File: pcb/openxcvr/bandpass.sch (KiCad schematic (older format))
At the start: 39 parts, among them U10 SN74CBT3253, U9 SN74CBT3253

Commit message: Candidate design
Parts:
- C30: renamed from C55; value 100nf -> 100n
- C33: renamed from C35; value 100nF -> 100n
- C34: renamed from C36; value 100nF -> 100n
- C35: renamed from C37; value 100nf -> 100n
- C36: renamed from C38; value 100nF -> 100n
- C49: renamed from C51; value 100nF -> 100n
- C50: renamed from C52; value 100nF -> 100n
- C51: renamed from C53; value 100nF -> 100n
- C52: renamed from C54; value 100nF -> 100n
- U8: renamed from U9; value SN74CBT3253 -> FST5253; symbol Analog_Switch:SN74CBT3253 -> xcvr_components:FST5253
- U9: renamed from U10; value SN74CBT3253 -> FST5253; symbol Analog_Switch:SN74CBT3253 -> xcvr_components:FST5253
- renumbered C33 to C31, C34 to C32, C39 to C37, C40 to C38, C41 to C39, C42 to C40, C43 to C41, C44 to C42, C45 to C43, C46 to C44, C47 to C45, C48 to C46, C49 to C47, C50 to C48, R31 to R30, R32 to R31
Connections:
- net labels added: RF_IN
- net labels removed: RF_OUT

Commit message: Get things working with rev 1 PCB
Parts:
- removed U8, U9: FST5253, Package_SO:SOIC-16_3.9x9.9mm_P1.27mm, symbol xcvr_components:FST5253
- added U8, U9: 74LS251, Package_SO:SOIC-16_3.9x9.9mm_P1.27mm, symbol 74xx:74LS251
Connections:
- net +5V: now also U8.16 (VCC), U9.16 (VCC)
- net BAND_0: now also U8.11 (S0), U9.11 (S0)
- net BAND_1: now also U8.10 (S1), U9.10 (S1)
- net BAND_2: now also U8.9 (S2), U9.9 (S2)
- net BPF_16_30_A: now also U8.4 (I0)
- net BPF_16_30_B: now also U9.4 (I0)
- net BPF_2_4_A: now also U8.1 (I3)
- net BPF_2_4_B: now also U9.1 (I3)
- net BPF_4_8_A: now also U8.2 (I2)
- net BPF_4_8_B: now also U9.2 (I2)
- net BPF_8_16_A: now also U8.3 (I1)
- net BPF_8_16_B: now also U9.3 (I1)
- net GND: now also U8.7 (~OE), U8.8 (GND), U9.7 (~OE), U9.8 (GND)
- net RF_BPF: now also U9.5 (Y)
- net at C30.2, R31.2: now also U8.5 (Y)
- new net: U8.12 (I7), U8.13 (I6), U8.14 (I5), U8.15 (I4), U9.12 (I7), U9.13 (I6), U9.14 (I5), U9.15 (I4)
- no-connect marks 4 -> 2
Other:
- moved on the sheet: C30, C31, C32, R30, R31

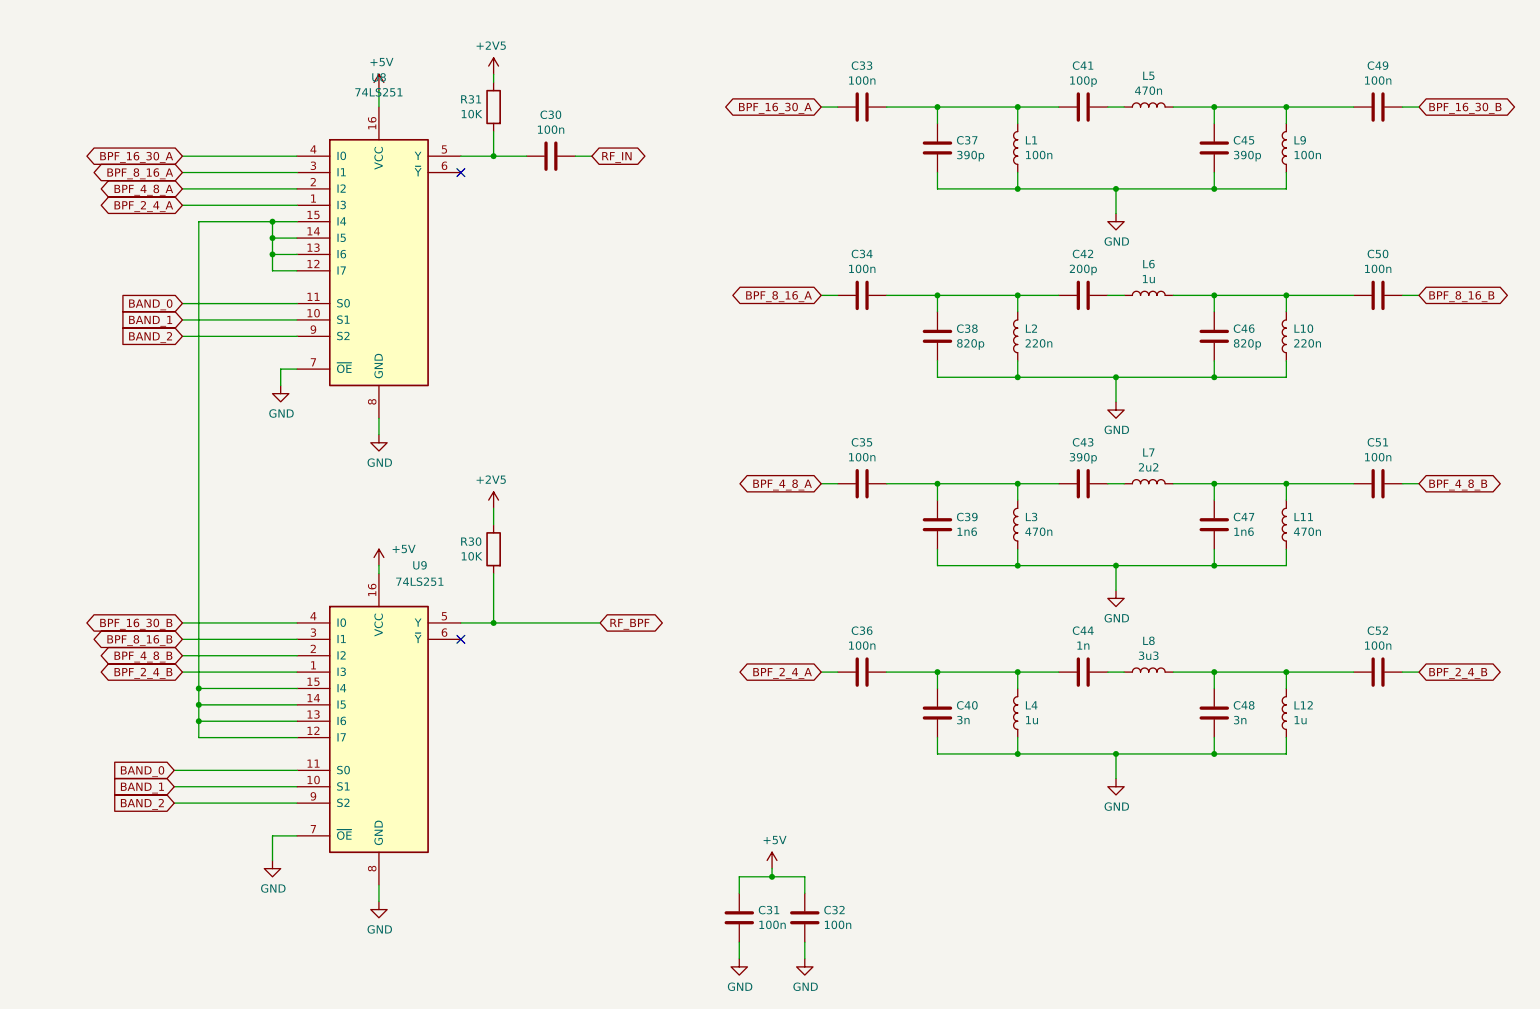
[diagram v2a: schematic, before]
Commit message: Add eeprom load store capability
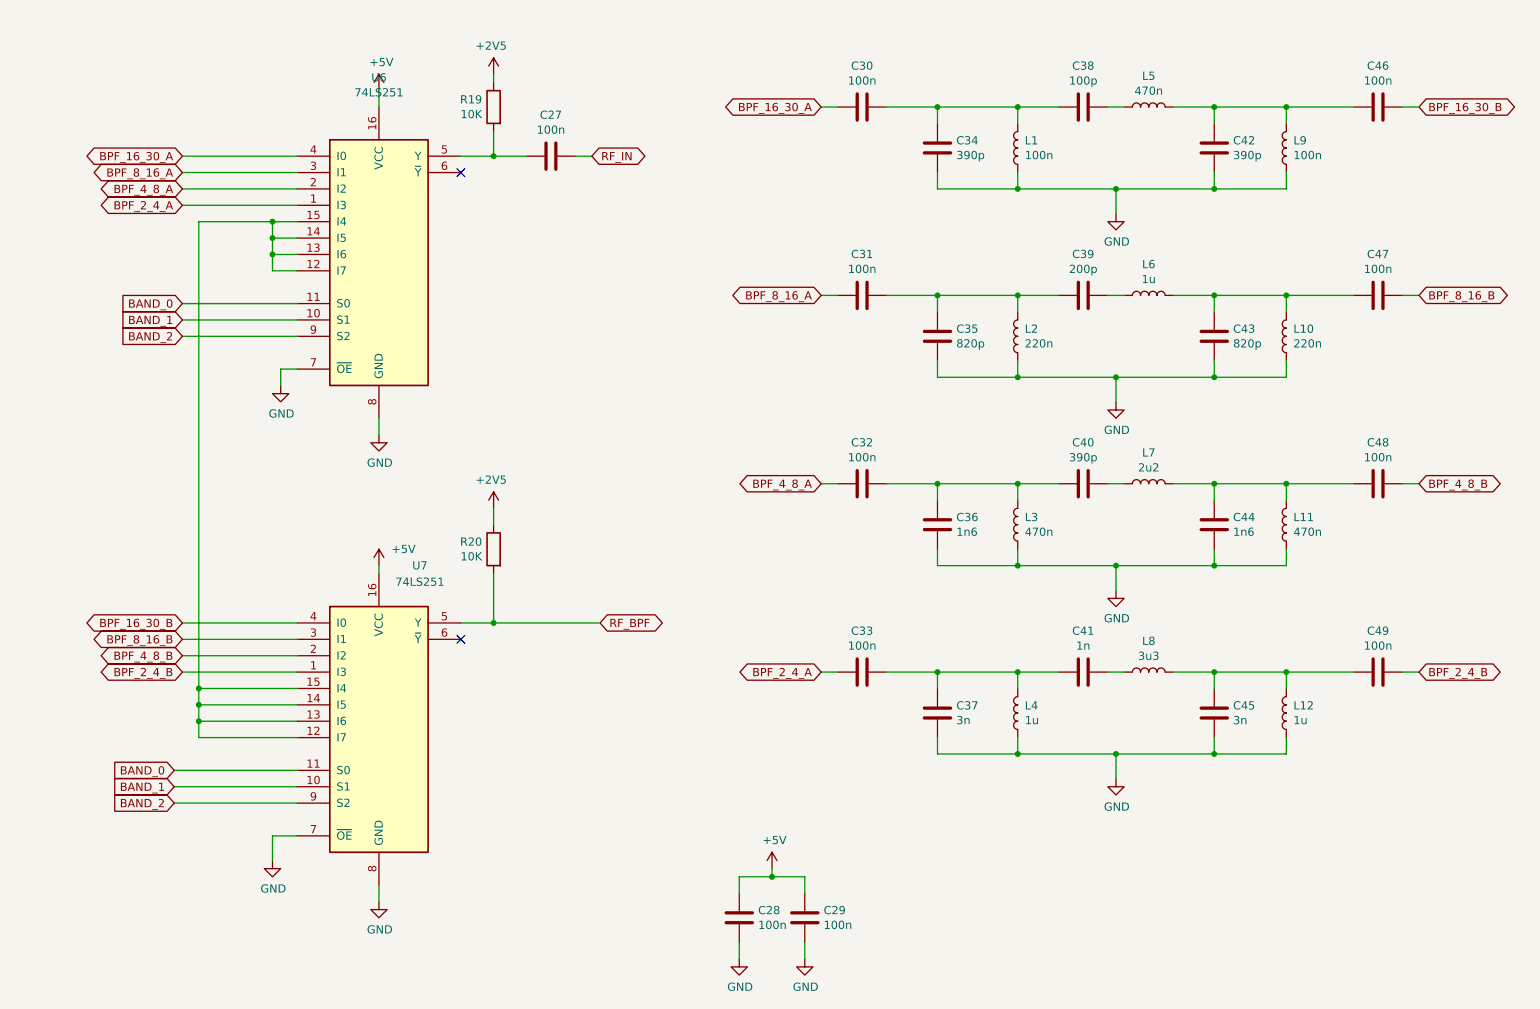
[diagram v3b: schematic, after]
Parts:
- renumbered C30 to C27, C31 to C28, C32 to C29, C33 to C30, C34 to C31, C35 to C32, C36 to C33, C37 to C34, C38 to C35, C39 to C36, C40 to C37, C41 to C38, C42 to C39, C43 to C40, C44 to C41, C45 to C42, C46 to C43, C47 to C44, C48 to C45, C49 to C46, C50 to C47, C51 to C48, C52 to C49, R31 to R19, R30 to R20, U8 to U6, U9 to U7
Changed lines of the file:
@@
 $Descr A4 11693 8268
 encoding utf-8
-Sheet 5 6
+Sheet 5 7
 Title "Open XCVR"
 Date "2020-01-26"
@@
 BPF_2_4_B
 $Comp
-L power:+5V #PWR0103
+L power:+5V #PWR053
 U 1 1 5E7853C6
 P 3200 1400
-F 0 "#PWR0103" H 3200 1250 50  0001 C CNN
+F 0 "#PWR053" H 3200 1250 50  0001 C CNN
 F 1 "+5V" H 3215 1573 50  0000 C CNN
 F 2 "" H 3200 1400 50  0001 C CNN
@@
 $EndComp
 $Comp
-L power:+5V #PWR0104
+L power:+5V #PWR055
 U 1 1 5E77FC3F
 P 3200 4300
-F 0 "#PWR0104" H 3200 4150 50  0001 C CNN
+F 0 "#PWR055" H 3200 4150 50  0001 C CNN
 F 1 "+5V" H 3350 4400 50  0000 C CNN
 F 2 "" H 3200 4300 50  0001 C CNN
@@
 $EndComp
 $Comp
-L power:+2V5 #PWR052
+L power:+2V5 #PWR057
 U 1 1 5E477A5B
 P 3900 1300
-F 0 "#PWR052" H 3900 1150 50  0001 C CNN
+F 0 "#PWR057" H 3900 1150 50  0001 C CNN
 F 1 "+2V5" H 3915 1473 50  0000 C CNN
 F 2 "" H 3900 1300 50  0001 C CNN
@@
 $EndComp
 $Comp
-L power:+2V5 #PWR051
+L power:+2V5 #PWR058
 U 1 1 5E4259F4
 P 3900 3950
-F 0 "#PWR051" H 3900 3800 50  0001 C CNN
+F 0 "#PWR058" H 3900 3800 50  0001 C CNN
 F 1 "+2V5" H 3915 4123 50  0000 C CNN
 F 2 "" H 3900 3950 50  0001 C CNN
@@
 $EndComp
 $Comp
-L power:GND #PWR0105
+L power:GND #PWR051
 U 1 1 5E76F28C
 P 2550 6100
-F 0 "#PWR0105" H 2550 5850 50  0001 C CNN
+F 0 "#PWR051" H 2550 5850 50  0001 C CNN
 F 1 "GND" H 2555 5927 50  0000 C CNN
 F 2 "" H 2550 6100 50  0001 C CNN
@@
 $EndComp
 $Comp
-L power:GND #PWR054
+L power:GND #PWR052
 U 1 1 5E3D4330
 P 2600 3200
-F 0 "#PWR054" H 2600 2950 50  0001 C CNN
+F 0 "#PWR052" H 2600 2950 50  0001 C CNN
 F 1 "GND" H 2605 3027 50  0000 C CNN
 F 2 "" H 2600 3200 50  0001 C CNN
@@
 $EndComp
 $Comp
-L power:GND #PWR0107
+L power:GND #PWR054
 U 1 1 5E779F26
 P 3200 3500
-F 0 "#PWR0107" H 3200 3250 50  0001 C CNN
+F 0 "#PWR054" H 3200 3250 50  0001 C CNN
 F 1 "GND" H 3205 3327 50  0000 C CNN
 F 2 "" H 3200 3500 50  0001 C CNN
@@
 $EndComp
 $Comp
-L power:GND #PWR0106
+L power:GND #PWR056
 U 1 1 5E76B51C
 P 3200 6350
-F 0 "#PWR0106" H 3200 6100 50  0001 C CNN
+F 0 "#PWR056" H 3200 6100 50  0001 C CNN
 F 1 "GND" H 3205 6177 50  0000 C CNN
 F 2 "" H 3200 6350 50  0001 C CNN
@@
 $EndComp
 $Comp
-L power:GND #PWR055
+L power:GND #PWR059
 U 1 1 5E4393E0
 P 5400 6700
-F 0 "#PWR055" H 5400 6450 50  0001 C CNN
+F 0 "#PWR059" H 5400 6450 50  0001 C CNN
 F 1 "GND" H 5405 6527 50  0000 C CNN
 F 2 "" H 5400 6700 50  0001 C CNN
@@
 $EndComp
 $Comp
-L Device:R R31
+L Device:R R19
 U 1 1 5E477A5A
 P 3900 1500
-F 0 "R31" H 3970 1545 50  0000 L CNN
+F 0 "R19" H 3970 1545 50  0000 L CNN
 F 1 "10K" H 3970 1455 50  0000 L CNN
 F 2 "Resistor_SMD:R_0805_2012Metric" V 3830 1500 50  0001 C CNN
@@
 $EndComp
 $Comp
-L Device:R R30
+L Device:R R20
 U 1 1 5E42415B
 P 3900 4200
-F 0 "R30" H 3970 4245 50  0000 L CNN
+F 0 "R20" H 3970 4245 50  0000 L CNN
 F 1 "10K" H 3970 4155 50  0000 L CNN
 F 2 "Resistor_SMD:R_0805_2012Metric" V 3830 4200 50  0001 C CNN
@@
 $EndComp
 $Comp
-L Device:C C30
+L Device:C C27
 U 1 1 5E45603E
 P 4250 1800
-F 0 "C30" V 4501 1800 50  0000 C CNN
+F 0 "C27" V 4501 1800 50  0000 C CNN
 F 1 "100n" V 4410 1800 50  0000 C CNN
 F 2 "Capacitor_SMD:C_0805_2012Metric" H 4288 1650 50  0001 C CNN
@@
 $EndComp
 $Comp
-L Device:C C31
+L Device:C C28
 U 1 1 5E390296
 P 5400 6450
-F 0 "C31" H 5515 6495 50  0000 L CNN
+F 0 "C28" H 5515 6495 50  0000 L CNN
 F 1 "100n" H 5515 6405 50  0000 L CNN
 F 2 "Capacitor_SMD:C_0805_2012Metric" H 5438 6300 50  0001 C CNN
@@
 $EndComp
 $Comp
-L Device:C C32
+L Device:C C29
 U 1 1 5E4393E1
 P 5800 6450
-F 0 "C32" H 5915 6495 50  0000 L CNN
+F 0 "C29" H 5915 6495 50  0000 L CNN
 F 1 "100n" H 5915 6405 50  0000 L CNN
 F 2 "Capacitor_SMD:C_0805_2012Metric" H 5838 6300 50  0001 C CNN
@@
 $EndComp
 $Comp
-L Device:C C33
+L Device:C C30
 U 1 1 5E451C79
 P 6150 1500
-F 0 "C33" V 6401 1500 50  0000 C CNN
+F 0 "C30" V 6401 1500 50  0000 C CNN
 F 1 "100n" V 6310 1500 50  0000 C CNN
 F 2 "Capacitor_SMD:C_0805_2012Metric" H 6188 1350 50  0001 C CNN
@@
 $EndComp
 $Comp
-L Device:C C34
+L Device:C C31
 U 1 1 5E472C6C
 P 6150 2650
-F 0 "C34" V 6401 2650 50  0000 C CNN
+F 0 "C31" V 6401 2650 50  0000 C CNN
 F 1 "100n" V 6310 2650 50  0000 C CNN
 F 2 "Capacitor_SMD:C_0805_2012Metric" H 6188 2500 50  0001 C CNN
@@
 $EndComp
 $Comp
-L Device:C C35
+L Device:C C32
 U 1 1 5E47C747
 P 6150 3800
-F 0 "C35" V 6401 3800 50  0000 C CNN
+F 0 "C32" V 6401 3800 50  0000 C CNN
 F 1 "100n" V 6310 3800 50  0000 C CNN
 F 2 "Capacitor_SMD:C_0805_2012Metric" H 6188 3650 50  0001 C CNN
@@
 $EndComp
 $Comp
-L Device:C C36
+L Device:C C33
 U 1 1 5E4A97D8
 P 6150 4950
-F 0 "C36" V 6401 4950 50  0000 C CNN
+F 0 "C33" V 6401 4950 50  0000 C CNN
 F 1 "100n" V 6310 4950 50  0000 C CNN
 F 2 "Capacitor_SMD:C_0805_2012Metric" H 6188 4800 50  0001 C CNN
@@
 $EndComp
 $Comp
-L Device:C C37
+L Device:C C34
 U 1 1 5E4437D6
 P 6610 1750
-F 0 "C37" H 6495 1705 50  0000 R CNN
+F 0 "C34" H 6495 1705 50  0000 R CNN
 F 1 "390p" H 6495 1795 50  0000 R CNN
 F 2 "Capacitor_SMD:C_0805_2012Metric" H 6648 1600 50  0001 C CNN
@@
 $EndComp
 $Comp
-L Device:C C38
+L Device:C C35
 U 1 1 5E472BA3
 P 6610 2900
-F 0 "C38" H 6495 2855 50  0000 R CNN
+F 0 "C35" H 6495 2855 50  0000 R CNN
 F 1 "820p" H 6495 2945 50  0000 R CNN
 F 2 "Capacitor_SMD:C_0805_2012Metric" H 6648 2750 50  0001 C CNN
@@
 $EndComp
 $Comp
-L Device:C C39
+L Device:C C36
 U 1 1 5E47C75C
 P 6610 4050
-F 0 "C39" H 6495 4005 50  0000 R CNN
+F 0 "C36" H 6495 4005 50  0000 R CNN
 F 1 "1n6" H 6495 4095 50  0000 R CNN
 F 2 "Capacitor_SMD:C_0805_2012Metric" H 6648 3900 50  0001 C CNN
@@
 $EndComp
 $Comp
-L Device:C C40
+L Device:C C37
 U 1 1 5E4A97A0
 P 6610 5200
-F 0 "C40" H 6495 5155 50  0000 R CNN
+F 0 "C37" H 6495 5155 50  0000 R CNN
 F 1 "3n" H 6495 5245 50  0000 R CNN
 F 2 "Capacitor_SMD:C_0805_2012Metric" H 6648 5050 50  0001 C CNN
@@
 $EndComp
 $Comp
-L Device:C C41
+L Device:C C38
 U 1 1 5E442FE2
 P 7500 1500
-F 0 "C41" V 7751 1500 50  0000 C CNN
+F 0 "C38" V 7751 1500 50  0000 C CNN
 F 1 "100p" V 7660 1500 50  0000 C CNN
 F 2 "Capacitor_SMD:C_0805_2012Metric" H 7538 1350 50  0001 C CNN
@@
 $EndComp
 $Comp
-L Device:C C42
+L Device:C C39
 U 1 1 5E472BC0
 P 7500 2650
-F 0 "C42" V 7751 2650 50  0000 C CNN
+F 0 "C39" V 7751 2650 50  0000 C CNN
 F 1 "200p" V 7660 2650 50  0000 C CNN
 F 2 "Capacitor_SMD:C_0805_2012Metric" H 7538 2500 50  0001 C CNN
@@
 $EndComp
 $Comp
-L Device:C C43
+L Device:C C40
 U 1 1 5E47C731
 P 7500 3800
-F 0 "C43" V 7751 3800 50  0000 C CNN
+F 0 "C40" V 7751 3800 50  0000 C CNN
 F 1 "390p" V 7660 3800 50  0000 C CNN
 F 2 "Capacitor_SMD:C_0805_2012Metric" H 7538 3650 50  0001 C CNN
@@
 $EndComp
 $Comp
-L Device:C C44
+L Device:C C41
 U 1 1 5E4A97B5
 P 7500 4950
-F 0 "C44" V 7751 4950 50  0000 C CNN
+F 0 "C41" V 7751 4950 50  0000 C CNN
 F 1 "1n" V 7660 4950 50  0000 C CNN
 F 2 "Capacitor_SMD:C_0805_2012Metric" H 7538 4800 50  0001 C CNN
@@
 $EndComp
 $Comp
-L Device:C C45
+L Device:C C42
 U 1 1 5E44671D
 P 8300 1750
-F 0 "C45" H 8185 1705 50  0000 R CNN
+F 0 "C42" H 8185 1705 50  0000 R CNN
 F 1 "390p" H 8185 1795 50  0000 R CNN
 F 2 "Capacitor_SMD:C_0805_2012Metric" H 8338 1600 50  0001 C CNN
@@
 $EndComp
 $Comp
-L Device:C C46
+L Device:C C43
 U 1 1 5E472BDF
 P 8300 2900
-F 0 "C46" H 8185 2855 50  0000 R CNN
+F 0 "C43" H 8185 2855 50  0000 R CNN
 F 1 "820p" H 8185 2945 50  0000 R CNN
 F 2 "Capacitor_SMD:C_0805_2012Metric" H 8338 2750 50  0001 C CNN
@@
 $EndComp
 $Comp
-L Device:C C47
+L Device:C C44
 U 1 1 5E47C6AD
 P 8300 4050
-F 0 "C47" H 8185 4005 50  0000 R CNN
+F 0 "C44" H 8185 4005 50  0000 R CNN
 F 1 "1n6" H 8185 4095 50  0000 R CNN
 F 2 "Capacitor_SMD:C_0805_2012Metric" H 8338 3900 50  0001 C CNN
@@
 $EndComp
 $Comp
-L Device:C C48
+L Device:C C45
 U 1 1 5E4A9741
 P 8300 5200
-F 0 "C48" H 8185 5155 50  0000 R CNN
+F 0 "C45" H 8185 5155 50  0000 R CNN
 F 1 "3n" H 8185 5245 50  0000 R CNN
 F 2 "Capacitor_SMD:C_0805_2012Metric" H 8338 5050 50  0001 C CNN
@@
 $EndComp
 $Comp
-L Device:C C49
+L Device:C C46
 U 1 1 5E458D26
 P 9300 1500
-F 0 "C49" V 9551 1500 50  0000 C CNN
+F 0 "C46" V 9551 1500 50  0000 C CNN
 F 1 "100n" V 9460 1500 50  0000 C CNN
 F 2 "Capacitor_SMD:C_0805_2012Metric" H 9338 1350 50  0001 C CNN
@@
 $EndComp
 $Comp
-L Device:C C50
+L Device:C C47
 U 1 1 5E472C25
 P 9300 2650
-F 0 "C50" V 9551 2650 50  0000 C CNN
+F 0 "C47" V 9551 2650 50  0000 C CNN
 F 1 "100n" V 9460 2650 50  0000 C CNN
 F 2 "Capacitor_SMD:C_0805_2012Metric" H 9338 2500 50  0001 C CNN
@@
 $EndComp
 $Comp
-L Device:C C51
+L Device:C C48
 U 1 1 5E47C6FA
 P 9300 3800
-F 0 "C51" V 9551 3800 50  0000 C CNN
+F 0 "C48" V 9551 3800 50  0000 C CNN
 F 1 "100n" V 9460 3800 50  0000 C CNN
 F 2 "Capacitor_SMD:C_0805_2012Metric" H 9338 3650 50  0001 C CNN
@@
 $EndComp
 $Comp
-L Device:C C52
+L Device:C C49
 U 1 1 5E4A972A
 P 9300 4950
-F 0 "C52" V 9551 4950 50  0000 C CNN
+F 0 "C49" V 9551 4950 50  0000 C CNN
 F 1 "100n" V 9460 4950 50  0000 C CNN
 F 2 "Capacitor_SMD:C_0805_2012Metric" H 9338 4800 50  0001 C CNN
@@
 $EndComp
 $Comp
-L 74xx:74LS251 U8
+L 74xx:74LS251 U6
 U 1 1 5E6F0B24
 P 3200 2400
-F 0 "U8" H 3200 3479 50  0000 C CNN
+F 0 "U6" H 3200 3479 50  0000 C CNN
 F 1 "74LS251" H 3200 3388 50  0000 C CNN
 F 2 "Package_SO:SOIC-16_3.9x9.9mm_P1.27mm" H 3200 2400 50  0001 C CNN
@@
 $EndComp
 $Comp
-L 74xx:74LS251 U9
+L 74xx:74LS251 U7
 U 1 1 5E723939
 P 3200 5250
-F 0 "U9" H 3450 6200 50  0000 C CNN
+F 0 "U7" H 3450 6200 50  0000 C CNN
 F 1 "74LS251" H 3450 6100 50  0000 C CNN
 F 2 "Package_SO:SOIC-16_3.9x9.9mm_P1.27mm" H 3200 5250 50  0001 C CNN

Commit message: Review and update schematic
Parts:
- U6, U7: value 74LS251 -> 74CBT3251
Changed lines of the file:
@@
 U 1 1 5E6F0B24
 P 3200 2400
-F 0 "U6" H 3200 3479 50  0000 C CNN
-F 1 "74LS251" H 3200 3388 50  0000 C CNN
+F 0 "U6" H 3800 2200 50  0000 C CNN
+F 1 "74CBT3251" H 3800 2100 50  0000 C CNN
 F 2 "Package_SO:SOIC-16_3.9x9.9mm_P1.27mm" H 3200 2400 50  0001 C CNN
 F 3 "http://www.ti.com/lit/gpn/sn74LS251" H 3200 2400 50  0001 C CNN
@@
 U 1 1 5E723939
 P 3200 5250
-F 0 "U7" H 3450 6200 50  0000 C CNN
-F 1 "74LS251" H 3450 6100 50  0000 C CNN
+F 0 "U7" H 3800 5350 50  0000 C CNN
+F 1 "74CBT3251" H 3800 5250 50  0000 C CNN
 F 2 "Package_SO:SOIC-16_3.9x9.9mm_P1.27mm" H 3200 5250 50  0001 C CNN
 F 3 "http://www.ti.com/lit/gpn/sn74LS251" H 3200 5250 50  0001 C CNN

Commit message: Review schematic and PCB layout
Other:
- note added: "Band 0 16-30 MHz"
- note added: "Band 1 8-16 MHz"
- note added: "Band 2 4-8 MHz"
- note added: "Band 3 2-4 MHz"
- note added: "Band 4-7 Bypass"
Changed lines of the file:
@@
 $Descr A4 11693 8268
 encoding utf-8
-Sheet 5 7
+Sheet 4 7
 Title "Open XCVR"
-Date "2020-01-26"
-Rev "0.1"
+Date "2020-06-14"
+Rev "0.2"
 Comp "Jon Dawson"
 Comment1 ""
@@
 Wire Wire Line
 	9450 4950 9550 4950
+Text Notes 10050 4150 2    50   ~ 0
+Band 2 4-8 MHz
+Text Notes 10050 5300 2    50   ~ 0
+Band 3 2-4 MHz
+Text Notes 10050 5850 2    50   ~ 0
+Band 4-7 Bypass
+Text Notes 10100 3050 2    50   ~ 0
+Band 1 8-16 MHz
+Text Notes 10150 1850 2    50   ~ 0
+Band 0 16-30 MHz
 Text GLabel 1950 5550 0    50   Input ~ 0
 BAND_0
